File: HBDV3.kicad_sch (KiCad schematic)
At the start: 56 parts, among them J1 RJ45 PWR, J2 Screw_Terminal_01x02 PWR, J3 RJ45 IN, J4 RJ45 OUT, J5 push_Terminal_01x04, J6 push_Terminal_01x04

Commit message: Changed diode, rough PCB layout
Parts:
- removed D1, D2, D3, D6, D7, D8: QH05BZ600, Package_TO_SOT_SMD:TO-263-2, symbol New_Library:QH05BZ600
- added D1, D2, D3, D6, D7, D8: PMEG10020ELRX, Diode_SMD:Nexperia_CFP3_SOD-123W, symbol Diode:PMEG10020ELR
- added H1, H2, H3, H4: MountingHole, MountingHole:MountingHole_4.3mm_M4_DIN965, symbol Mechanical:MountingHole
- added J2: RJ45 PWR, Library:RJ45_E5J8800LJG2L, symbol Connector:RJ45
- renumbered J2 to J3, J3 to J4, J4 to J5, J5 to J6, J6 to J7
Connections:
- net +16.5V: now also J2.2, J2.4, J2.6, J2.8
- net GND: now also J2.1, J2.3, J2.5, J2.7
- net VDDA: now also D3.1 (K)
- net VDDA_B: now also D8.1 (K)
- net VOUTA: now also D1.2 (A)
- net VOUTA_B: now also D6.2 (A)
- net VOUTB: now also D2.2 (A)
- net VOUTB_B: now also D7.2 (A)
- net at R18.2, R19.2: now also D7.1 (K)
- net at R6.2, R7.2: now also D2.1 (K)
- net at R14.2, R15.2: now also D6.1 (K)
- net at R22.2: now also D8.2 (A)
- net at R10.2: now also D3.2 (A)
- net at R2.2, R3.2: now also D1.1 (K)
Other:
- moved on the sheet: J3

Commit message: Finished layout, added silkscreen text, configured track width
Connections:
- net STP U2: now reaches R13.2, U2.6 (STP/DTC)
- net STP U1: now reaches R1.2, U1.6 (STP/DTC)
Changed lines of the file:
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@@
+		)
+	)
+	(label "STP U1"
+		(at 48.26 86.36 180)
+		(effects
+			(font
+				(size 1.27 1.27)
+			)
+			(justify right bottom)
 		)
 	)
@@
 		(effects
 			(font
+				(size 1.27 1.27)
+			)
+			(justify right bottom)
+		)
+	)
+	(label "STP U2"
+		(at 185.42 86.36 180)
+		(effects
+			(font

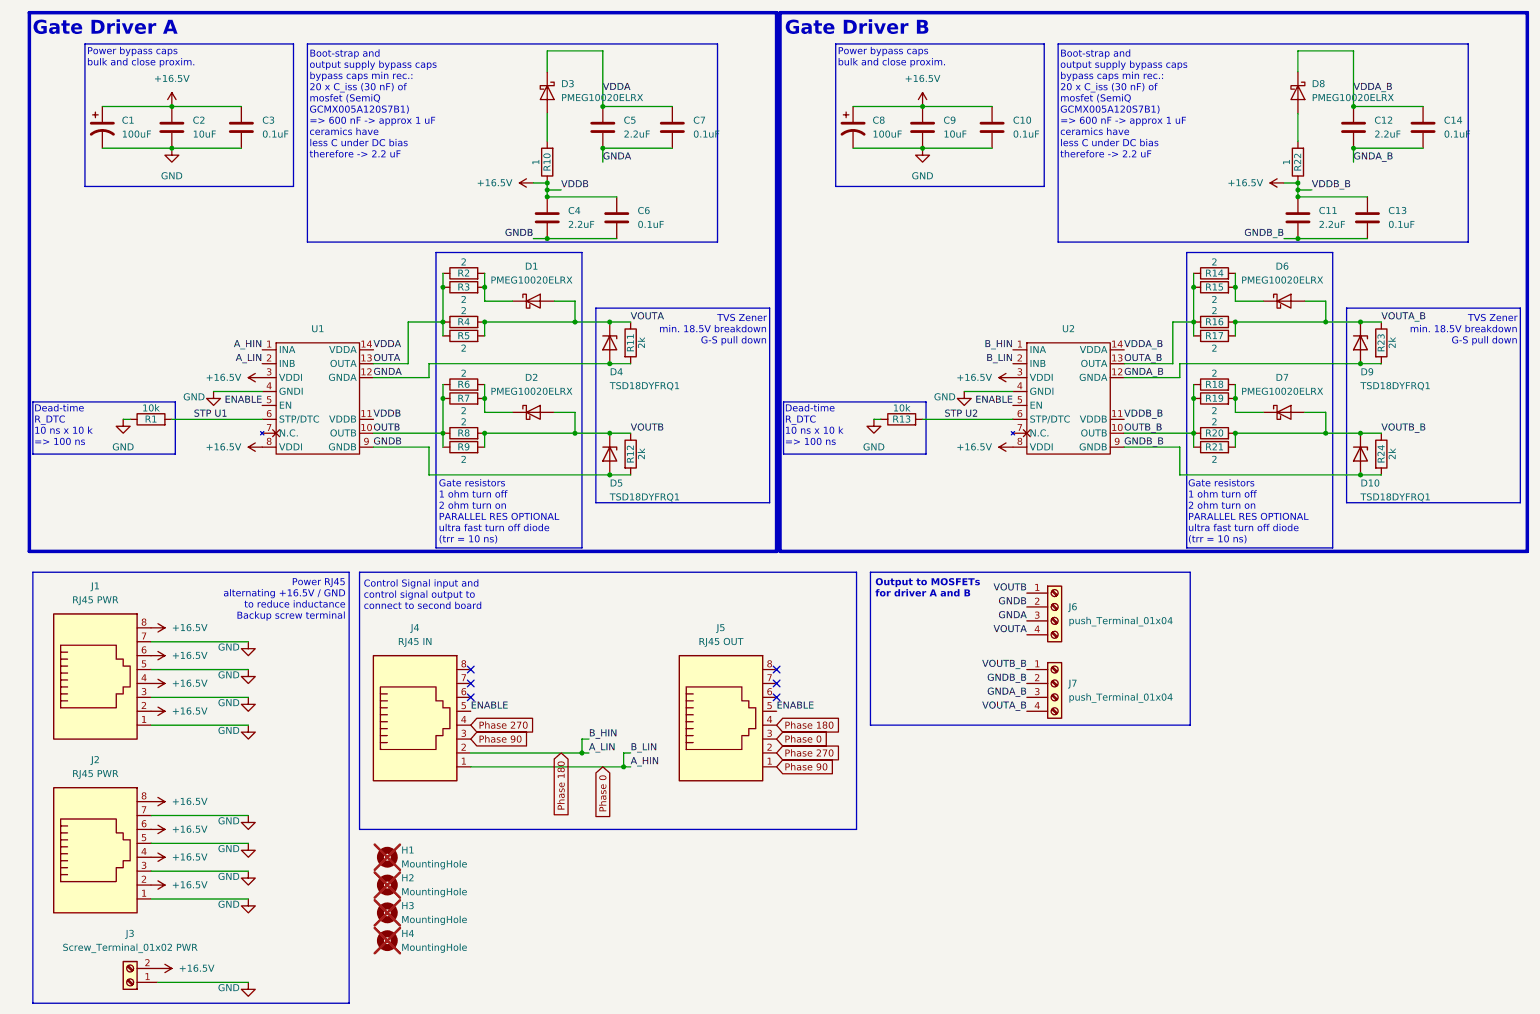
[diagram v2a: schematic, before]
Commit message: Updated sig in/out for phase splitter compatibility + zener series R
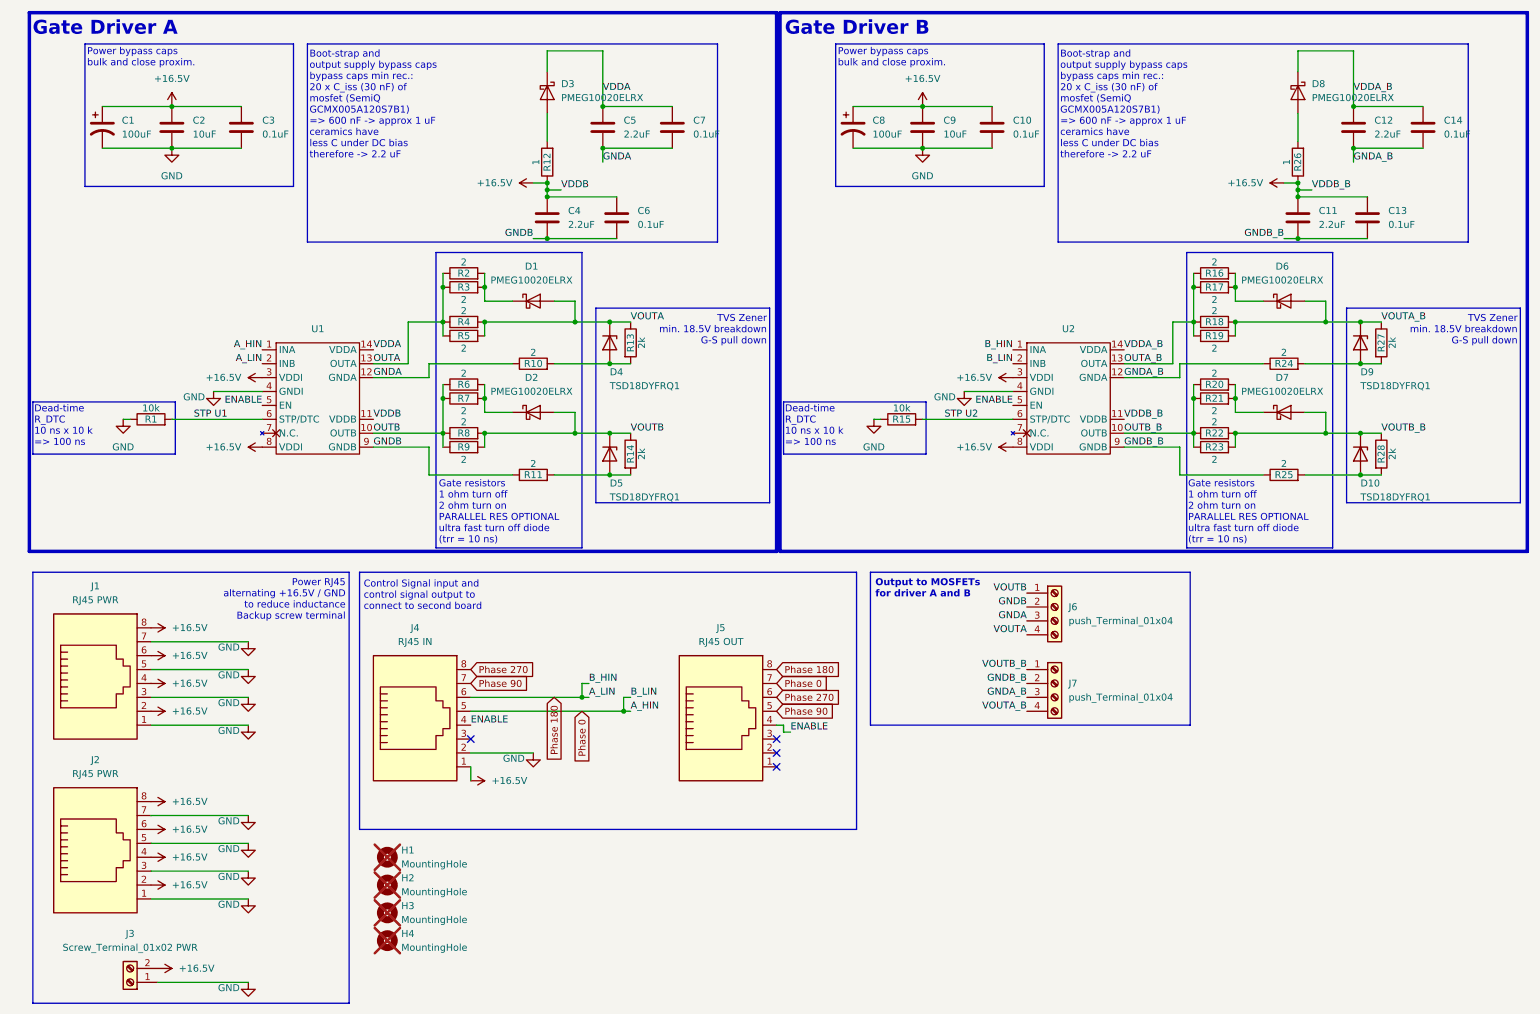
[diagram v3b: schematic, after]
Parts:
- added R10, R11, R24, R25: 2, Resistor_SMD:R_2512_6332Metric_Pad1.40x3.35mm_HandSolder, symbol Device:R
- renumbered R10 to R12, R11 to R13, R12 to R14, R13 to R15, R14 to R16, R15 to R17, R16 to R18, R17 to R19, R18 to R20, R19 to R21, R20 to R22, R21 to R23, R22 to R26, R23 to R27, R24 to R28
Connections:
- net +16.5V: now also J4.1
- net ENABLE: now also J4.4, J5.4; no longer J4.5, J5.5
- net GND: now also J4.2
- net GNDA: now also R10.1; no longer D4.2 (A), R13.2
- net GNDA_B: now also R24.1; no longer D9.2 (A), R27.2
- net GNDB: now also R11.1; no longer D5.2 (A), R14.2
- net GNDB_B: now also R25.1; no longer D10.2 (A), R28.2
- net Phase 0: now also J4.5, J5.7; no longer J4.1, J5.3
- net Phase 180: now also J4.6, J5.8; no longer J4.2, J5.4
- net Phase 270: now also J4.8, J5.6; no longer J4.4, J5.2
- net Phase 90: now also J4.7, J5.5; no longer J4.3, J5.1
- new net: D4.2 (A), R10.2, R13.2
- new net: D9.2 (A), R24.2, R27.2
- new net: D10.2 (A), R25.2, R28.2
- new net: D5.2 (A), R11.2, R14.2
- no-connect marks 6 -> 4

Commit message: Gerber files and 4.7uF cap adjustment
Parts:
- C11, C12, C4, C5: value 2.2uF -> 4.7uF; Digikey https://www.digikey.ca/en/products/detail/samsung-electro-m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 -> https://www.digikey.ca/en/products/detail/murata-electronic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
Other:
- note added: "Boot-strap and output supply bypass caps bypass caps min rec.: 20 x C_iss (30 nF) of mosfet (SemiQ GCMX005A120S7B1) => 600 nF -> approx 1 uF ceramics have less C under DC bias -80% -> 4.7 uF"
- note added: "Gate resistors 1 ohm turn off 2 ohm turn on PARALLEL RES OPTIONAL ultra fast turn off diode (trr < 10 ns)"
- note removed: "Gate resistors 1 ohm turn off 2 ohm turn on PARALLEL RES OPTIONAL ultra fast turn off diode (trr = 10 ns)"
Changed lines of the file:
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@@
 		)
 	)
-	(text "Gate resistors\n1 ohm turn off\n2 ohm turn on\nPARALLEL RES OPTIONAL\nultra fast turn off diode \n(trr = 10 ns)"
+	(text "Gate resistors\n1 ohm turn off\n2 ohm turn on\nPARALLEL RES OPTIONAL\nultra fast turn off diode \n(trr < 10 ns)"
 		(exclude_from_sim no)
 		(at 223.774 103.378 0)
@@
 		)
 	)
-	(text "Gate resistors\n1 ohm turn off\n2 ohm turn on\nPARALLEL RES OPTIONAL\nultra fast turn off diode \n(trr = 10 ns)"
+	(text "Gate resistors\n1 ohm turn off\n2 ohm turn on\nPARALLEL RES OPTIONAL\nultra fast turn off diode \n(trr < 10 ns)"
 		(exclude_from_sim no)
 		(at 86.868 103.378 0)
@@
 		)
 	)
-	(text "Boot-strap and\noutput supply bypass caps\nbypass caps min rec.:\n20 x C_iss (30 nF) of \nmosfet (SemiQ \nGCMX005A120S7B1) \n=> 600 nF -> approx 1 uF\nceramics have\nless C under DC bias\ntherefore -> 2.2 uF"
+	(text "Boot-strap and\noutput supply bypass caps\nbypass caps min rec.:\n20 x C_iss (30 nF) of \nmosfet (SemiQ \nGCMX005A120S7B1) \n=> 600 nF -> approx 1 uF\nceramics have\nless C under DC bias\n-80% -> 4.7 uF"
 		(exclude_from_sim no)
 		(at 63.246 28.956 0)
@@
 			)
 		)
-		(property "Value" "2.2uF"
+		(property "Value" "4.7uF"
 			(at 257.81 34.2899 0)
 			(show_name no)
@@
 			)
 		)
-		(property "Digikey" "https://www.digikey.ca/en/products/detail/samsung-electro-mechanics/CL21A225KBFNNNE/5961186"
+		(property "Digikey" "https://www.digikey.ca/en/products/detail/murata-electronics/GRM21BR61H475KE51L/4905540"
 			(at 254 33.02 0)
 			(hide yes)
@@
 			)
 		)
-		(property "Value" "2.2uF"
+		(property "Value" "4.7uF"
 			(at 120.65 34.2899 0)
 			(show_name no)
@@
 			)
 		)
-		(property "Digikey" "https://www.digikey.ca/en/products/detail/samsung-electro-mechanics/CL21A225KBFNNNE/5961186"
+		(property "Digikey" "https://www.digikey.ca/en/products/detail/murata-electronics/GRM21BR61H475KE51L/4905540"
 			(at 116.84 33.02 0)
 			(hide yes)
@@
 			)
 		)
-		(property "Value" "2.2uF"
+		(property "Value" "4.7uF"
 			(at 247.65 50.7999 0)
 			(show_name no)
@@
 			)
 		)
-		(property "Digikey" "https://www.digikey.ca/en/products/detail/samsung-electro-mechanics/CL21A225KBFNNNE/5961186"
+		(property "Digikey" "https://www.digikey.ca/en/products/detail/murata-electronics/GRM21BR61H475KE51L/4905540"
 			(at 243.84 49.53 0)
 			(hide yes)
@@
 			)
 		)
-		(property "Value" "2.2uF"
+		(property "Value" "4.7uF"
 			(at 110.49 50.7999 0)
 			(show_name no)
@@
 			)
 		)
-		(property "Digikey" "https://www.digikey.ca/en/products/detail/samsung-electro-mechanics/CL21A225KBFNNNE/5961186"
+		(property "Digikey" "https://www.digikey.ca/en/products/detail/murata-electronics/GRM21BR61H475KE51L/4905540"
 			(at 106.68 49.53 0)
 			(hide yes)
